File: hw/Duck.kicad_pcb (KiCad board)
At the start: 2 copper layers, 35.5 x 20.8 mm, 36 parts, among them J1 Conn_01x06, J2 Conn_01x04, J3 USB_C_Receptacle_USB2.0_14P, J4 Conn_01x06, Q1 MMBT3904, Q2 MMBT3904, U1 ESP32-S3-MINI-1, U2 SPX3819M5-L-3-3, U3 INMP441, U4 MAX17048G+T10, U5 CH343P

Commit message: hw: 🚧 Revision
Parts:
- added AE1: 2.4GHz 50R, Duck_footprints:ANT_IFA_USB_2.4GHz_50R, F.Cu at (58.6, 49.5)
- added C3: 1u, Capacitor_SMD:C_0402_1005Metric, F.Cu at (59.9, 53.4)
- added C4: 0 TBD, Capacitor_SMD:C_0402_1005Metric, F.Cu at (60.3, 46.5)
- added C5: 0 TBD, Capacitor_SMD:C_0402_1005Metric, F.Cu at (60.3, 49.2)
- added C6: 100n, Capacitor_SMD:C_0402_1005Metric, B.Cu at (66.3, 51.8)
- added C7: 6.8p, Capacitor_SMD:C_0402_1005Metric, B.Cu at (63.1, 57.9)
- added C8: 6.8p, Capacitor_SMD:C_0402_1005Metric, B.Cu at (66.8, 57.9)
- added L1: 0 TBD, Inductor_SMD:L_0402_1005Metric, F.Cu at (60.8, 47.9)
- added R1: 10k, Resistor_SMD:R_0402_1005Metric, F.Cu at (58.9, 53.4)
- added U2: PY32F003F1xU6, Package_DFN_QFN:QFN-20-1EP_3x3mm_P0.4mm_EP1.65x1.65mm, B.Cu at (64.8, 54.6)
- added Y1: 32MHz 12pF, Crystal:Crystal_SMD_2016-4Pin_2.0x1.6mm, B.Cu at (65.0, 58.0)
- BT1, C1, C2: moved to F.Cu
- C10: renamed from C4; moved to F.Cu
- C11: renamed from C5; moved to B.Cu
- C9: renamed from C3; moved to F.Cu
- D1: footprint LED_THT:LED_D5.0mm-4_RGB -> Duck_footprints:LED_1x04_D5.0_P1.27
- J2: footprint Duck_footprints:SMD_1x04_P2.54mm -> Duck_footprints:TestPoints_1x04_P2.0; moved to F.Cu
- R4: renamed from R3; moved to B.Cu
- R5: renamed from R4; moved to B.Cu
- R6: renamed from R5; moved to B.Cu
- U1: value ESP32-S3-MINI-1 -> ESP32-S3-PICO-1; footprint Espressif:ESP32-S3-MINI-1 -> Espressif:ESP32-S3-PICO-1-LGA-56
- U3: renamed from U2; moved to F.Cu
- U4: renamed from U3; moved to B.Cu
- moved J1 28.8 mm to (44.3, 44.8), turned to 0 degrees
- moved J2 17.5 mm to (41.1, 38.4), turned to 0 degrees
- moved C1 10.3 mm to (58.9, 51.6)
- moved C2 10.3 mm to (59.9, 51.6)
- moved C12 9.75 mm to (73.3, 53.5), turned to -90 degrees
- moved D1 9.32 mm to (71.4, 58.1)
- moved C10 8.51 mm to (72.8, 50.9), turned to -90 degrees
- moved C9 8.11 mm to (72.8, 52.8), turned to -90 degrees
- moved U1 7.32 mm to (64.0, 53.5)
- moved R4 6.92 mm to (69.6, 56.2)
- moved R5 6.92 mm to (71.4, 56.2)
- moved R6 6.92 mm to (73.3, 56.2)
- moved U5 6.15 mm to (71.2, 53.3), turned to 180 degrees
- moved R2 5.72 mm to (69.1, 53.8), turned to 90 degrees
- moved R3 5.04 mm to (68.2, 53.2), turned to 90 degrees
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- renumbered C6 to C12, C7 to C13, C8 to C14, C9 to C15, R9 to R10, R10 to R11, R1 to R2, R2 to R3, R6 to R7, R7 to R8, R8 to R9, U4 to U5, U5 to U6
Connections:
- J2 pad 3: /GNSS_TX -> /SWDIO
- J2 pad 4: /GNSS_RX -> /SWCLK
- U1 pad 1: GND -> Net-(U1-LNA_IN)
- U1 pad 12: /GNSS_TX -> unconnected-(U1-GPIO7-Pad12)
- U1 pad 13: /GNSS_RX -> unconnected-(U1-GPIO8-Pad13)
- U1 pad 16: /MIC_WS -> unconnected-(U1-GPIO11-Pad16)
- U1 pad 17: /MIC_SD -> unconnected-(U1-GPIO12-Pad17)
- U1 pad 18: /MIC_SCK -> unconnected-(U1-GPIO13-Pad18)
- U1 pad 19: /MIC_EN -> unconnected-(U1-GPIO14-Pad19)
- U1 pad 2: GND -> +3V3
- U1 pad 20: unconnected-(U1-GPIO16/U0CTS/ADC2_CH5/XTAL_32K_N-Pad20) -> +3V3
- U1 pad 21: /LED_R -> unconnected-(U1-GPIO15/XTAL_32K_P-Pad21)
- U1 pad 22: /LED_G -> unconnected-(U1-GPIO16/XTAL_32K_N-Pad22)
- U1 pad 25: /LED_B -> unconnected-(U1-USB_D-/GPIO19-Pad25)
- U1 pad 31: /SDA -> unconnected-(U1-SPIWP/NC-Pad31)
- U1 pad 32: /SCL -> unconnected-(U1-SPICS0/NC-Pad32)
- U1 pad 39: /U0TXD -> /SER_UP
- U1 pad 4: /BOOT0 -> /ESP_EN
- U1 pad 40: /U0RXD -> /SER_DN
- U1 pad 42: GND -> unconnected-(U1-GPIO37-Pad42)
- U1 pad 43: GND -> unconnected-(U1-GPIO38-Pad43)
- U1 pad 45: /ESP_EN -> unconnected-(U1-MTDO/GPIO40-Pad45)
- U1 pad 46: GND -> unconnected-(U1-VDD_CPU-Pad46)
- U1 pad 47: GND -> unconnected-(U1-MTDI/GPIO41-Pad47)
- U1 pad 48: GND -> unconnected-(U1-MTMS/GPIO42-Pad48)
- U1 pad 49: GND -> /U0TXD
- U1 pad 5: unconnected-(U1-GPIO1/TOUCH1/ADC1_CH0-Pad5) -> /BOOT0
- U1 pad 50: GND -> /U0RXD
- U1 pad 51: GND -> unconnected-(U1-GPIO45-Pad51)
- U1 pad 52: GND -> unconnected-(U1-GPIO46-Pad52)
- U1 pad 53: GND -> unconnected-(U1-XTAL_N/NC-Pad53)
- U1 pad 54: GND -> unconnected-(U1-XTAL_P/NC-Pad54)
- U1 pad 55: GND -> +3V3
- U1 pad 56: GND -> +3V3
- U4 pad 8: /MIC_EN -> +3V3
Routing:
- net +3V3: track 41.0 -> 2.71 mm, vias 2 -> 0
- net /BOOT0: track 32.5 -> 15.8 mm, vias 2 -> 0
- net +BATT: track 37.3 -> 23.8 mm, vias 2 -> 1
- net /MIC_EN: track 5.05 -> 0.00 mm
- net /SCL: track 5.63 -> 1.19 mm, vias 1 -> 0
- net /ESP_EN: track 17.9 -> 13.6 mm
- net /SDA: track 5.77 -> 2.13 mm, vias 1 -> 0
- net /U0TXD: track 16.6 -> 14.3 mm
- net Net-(D1-BK): track 2.18 -> 0.00 mm
- net /MIC_SCK: track 1.95 -> 0.00 mm
- net Net-(D1-GK): track 1.94 -> 0.00 mm
- net /MIC_SD: track 1.87 -> 0.00 mm
- net Net-(D1-RK): track 1.80 -> 0.00 mm
- net /MIC_WS: track 1.79 -> 0.00 mm
- net /U0RXD: track 14.4 -> 12.6 mm
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- removed copper zone on B.Cu, net +3V3

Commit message: hw: 🚧 Adjustments; layout?
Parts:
- removed C4, C5: 0 TBD, Capacitor_SMD:C_0402_1005Metric
- removed L1: 0 TBD, Inductor_SMD:L_0402_1005Metric
- removed R2, R3: 4.7k, Resistor_SMD:R_0402_1005Metric
- BT1: moved to B.Cu
- D1, R4, R5, R6: moved to F.Cu
- Y1: value 32MHz 12pF -> 24.576MHz 12pF
- moved C6 6.96 mm to (64.0, 58.4), turned to 0 degrees
- moved C8 6.66 mm to (62.9, 52.5), turned to -90 degrees
- moved C7 6.51 mm to (66.6, 52.5), turned to 90 degrees
- moved Y1 5.51 mm to (64.7, 52.5), turned to 0 degrees
- moved C12 3.22 mm to (70.4, 52.1), turned to 0 degrees
- moved U5 2.77 mm to (68.4, 53.1), turned to -90 degrees
- moved C1 2.17 mm to (60.0, 53.5)
- moved C2 2.17 mm to (60.9, 53.5)
- moved C3 2.17 mm to (60.9, 55.3)
- moved R1 2.17 mm to (60.0, 55.3)
- moved U1 2.17 mm to (65.1, 55.3)
- moved C10 1.99 mm to (73.5, 52.7)
- moved C9 1.99 mm to (73.5, 54.6)
- moved U3 1.99 mm to (71.0, 53.2)
- moved AE1 1.93 mm to (59.7, 51.1)
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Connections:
- AE1 pad 1: Net-(AE1-Pad1) -> Net-(U1-LNA_IN)
- U1 pad 27: unconnected-(U1-GPIO21-Pad27) -> /SER_DN
- U1 pad 36: unconnected-(U1-GPIO48/SPICLK_N-Pad36) -> /SER_UP
- U1 pad 39: /SER_UP -> unconnected-(U1-GPIO34-Pad39)
- U1 pad 40: /SER_DN -> unconnected-(U1-GPIO35-Pad40)
- U2 pad 1: /LED_R -> /LED_B
- U2 pad 10: /SER_UP -> /MIC_SCK
- U2 pad 11: /SER_DN -> unconnected-(U2-PB7-Pad11)
- U2 pad 12: unconnected-(U2-PF4-Pad12) -> /SDA
- U2 pad 15: unconnected-(U2-PF2-Pad15) -> /SCL
- U2 pad 16: /MIC_SD -> /SER_UP
- U2 pad 17: /MIC_SCK -> /SER_DN
- U2 pad 18: /SDA -> /LED_R
- U2 pad 19: /SCL -> unconnected-(U2-PA3-Pad19)
- U2 pad 2: /LED_B -> /MIC_SD
- U4 pad 4: +3V3 -> GND
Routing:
- net /MIC_SD: track 0.00 -> 12.8 mm
- net /SDA: track 2.13 -> 12.5 mm
- net /LED_B: track 0.00 -> 7.98 mm, vias 0 -> 1
- net /LED_R: track 0.00 -> 7.18 mm, vias 0 -> 1
- net /LED_G: track 0.00 -> 5.66 mm, vias 0 -> 1
- net /MIC_WS: track 0.00 -> 5.65 mm
- net +3V3: track 2.71 -> 7.90 mm
- net +BATT: track 23.8 -> 28.6 mm, vias 1 -> 0
- net /SER_DN: track 0.00 -> 4.18 mm, vias 0 -> 1
- net Net-(U1-LNA_IN): track 0.00 -> 4.10 mm
- net Net-(U2-PF0): track 0.00 -> 2.87 mm
- net Net-(D1-BK): track 0.00 -> 2.13 mm
- net Net-(D1-RK): track 0.00 -> 2.08 mm
- net /SER_UP: track 0.00 -> 2.01 mm, vias 0 -> 1
- net Net-(D1-GK): track 0.00 -> 1.94 mm
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
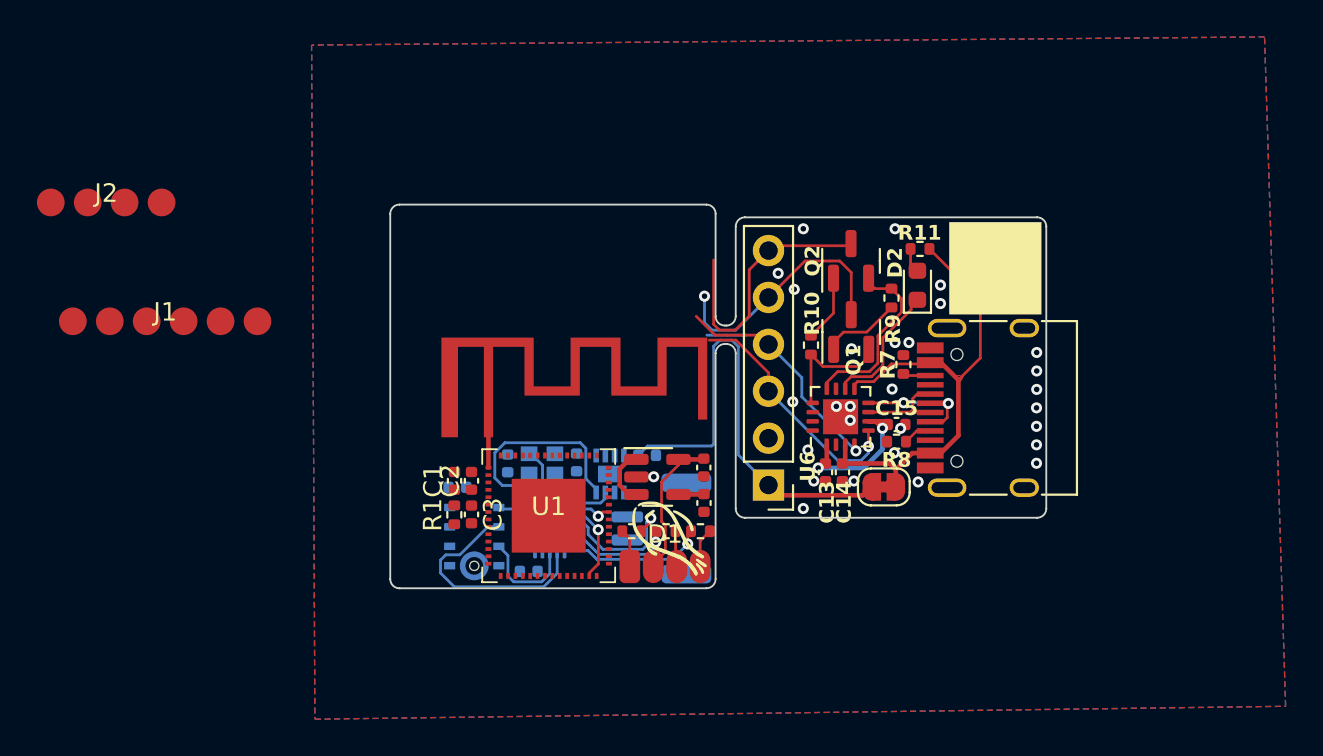
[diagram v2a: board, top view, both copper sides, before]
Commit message: hw: 🚧 Do we give up this small form factor?
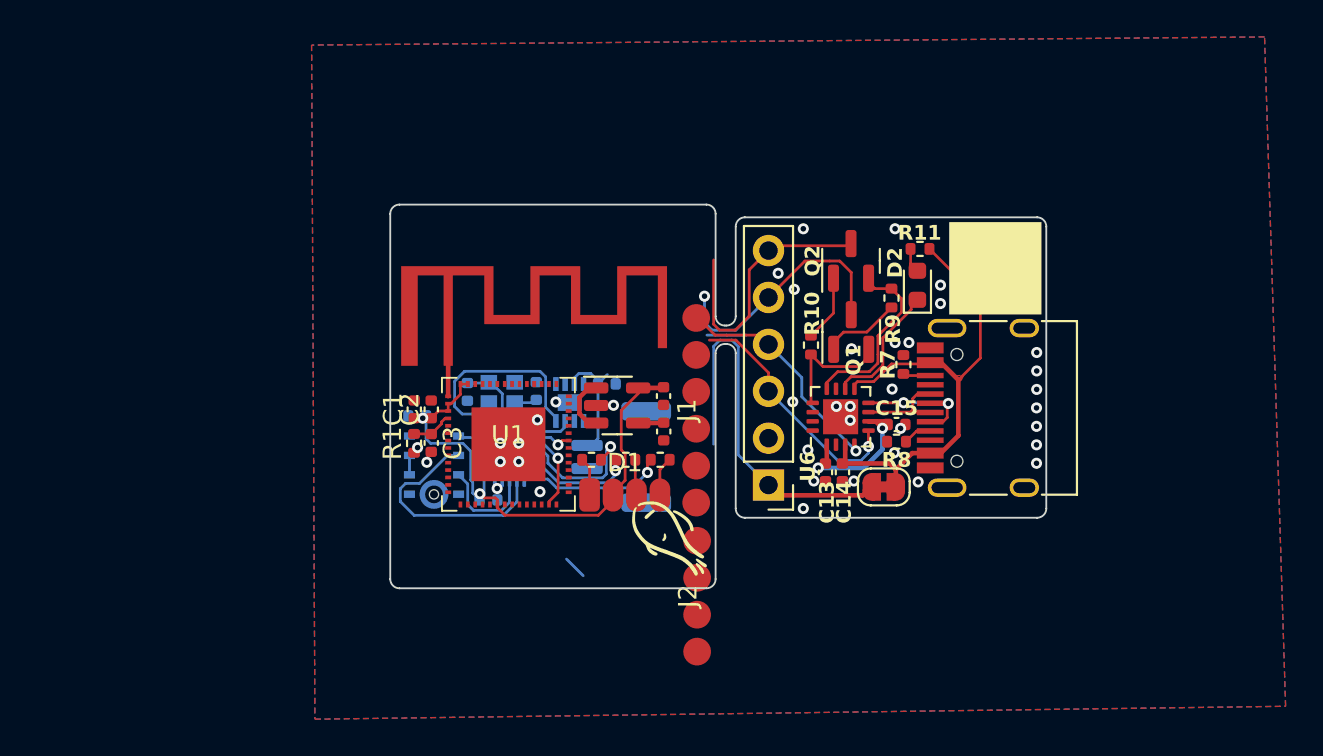
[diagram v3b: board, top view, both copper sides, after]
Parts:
- moved J2 38.5 mm to (73.1, 59.7), turned to 90 degrees
- moved J1 29.2 mm to (73.1, 49.6), turned to 90 degrees
- moved D1 4.44 mm to (69.2, 54.2)
- moved C1 4.44 mm to (57.8, 49.6)
- moved C11 4.44 mm to (58.0, 49.9)
- moved C2 4.44 mm to (58.7, 49.6)
- moved C3 4.44 mm to (58.7, 51.4)
- moved C8 4.44 mm to (60.7, 48.6)
- moved C10 4.44 mm to (71.3, 48.9)
- moved C12 4.44 mm to (68.2, 48.2)
- moved C9 4.44 mm to (71.3, 50.8)
- moved U5 4.44 mm to (66.2, 49.2)
- moved BT1 4.44 mm to (69.0, 52.2)
- moved U1 4.44 mm to (62.9, 51.5)
- moved U3 4.44 mm to (68.8, 49.4)
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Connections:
- U2 pad 5: unconnected-(U2-PA12-Pad5) -> GND
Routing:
- net +3V3: track 7.90 -> 31.6 mm, vias 0 -> 3
- net Net-(U2-PF1): track 0.00 -> 2.52 mm
- net /ESP_EN: track 13.6 -> 15.9 mm
- net /MIC_SD: track 12.8 -> 14.9 mm
- net GND: track 2.13 -> 0.00 mm, vias 29 -> 38
- net +BATT: track 28.6 -> 30.7 mm
- net Net-(U2-PF0): track 2.87 -> 4.04 mm

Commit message: hw: Further simplify 🚧
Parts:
- removed the C6 at (61.8, 54.5)
- removed the C7 at (64.4, 48.6)
- removed the C8 at (60.7, 48.6)
- removed the J2 at (73.1, 59.7)
- removed the U2 at (63.0, 51.9)
- removed Y1: 24.576MHz 12pF, Crystal:Crystal_SMD_2016-4Pin_2.0x1.6mm
- added R2: 4.7k, Resistor_SMD:R_0402_1005Metric, B.Cu at (65.2, 53.1)
- added R3: 4.7k, Resistor_SMD:R_0402_1005Metric, B.Cu at (64.7, 52.2)
- moved J1 4.09 mm to (73.1, 45.5)
- moved C7 2.14 mm to (66.6, 49.6), turned to -90 degrees
- moved U4 1.58 mm to (64.9, 50.1)
- moved R6 0.83 mm to (70.3, 52.1), turned to -90 degrees
- moved R4 0.36 mm to (67.7, 52.0), turned to -90 degrees
- moved BT1 0.34 mm to (68.9, 51.8)
- moved C6 0.27 mm to (58.0, 49.7)
- moved U3 0.27 mm to (58.9, 52.3)
- moved R5 0.26 mm to (69.4, 52.1), turned to -90 degrees
- moved D1 0.19 mm to (69.2, 54.0)
- moved R1 0.09 mm to (57.7, 51.4)
- renumbered C15 to C10, C9 to C4, C10 to C5, C11 to C6, C12 to C7, C13 to C8, C14 to C9, J4 to J2, U3 to U2, U4 to U3, U5 to U4, U6 to U5
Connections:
- U1 pad 25: unconnected-(U1-USB_D-/GPIO19-Pad25) -> /SDA
- U1 pad 26: unconnected-(U1-USB_D+/GPIO20-Pad26) -> /SCL
- U1 pad 27: /SER_DN -> unconnected-(U1-GPIO21-Pad27)
- U1 pad 36: /SER_UP -> /LED_B
- U1 pad 37: unconnected-(U1-GPIO47/SPICLK_P-Pad37) -> /LED_R
- U1 pad 38: unconnected-(U1-GPIO33-Pad38) -> /LED_G
- U1 pad 6: unconnected-(U1-GPIO1-Pad6) -> /MIC_SCK
- U1 pad 7: unconnected-(U1-GPIO2-Pad7) -> /MIC_SCK
- U1 pad 8: unconnected-(U1-GPIO3-Pad8) -> /MIC_SD
- U1 pad 9: unconnected-(U1-GPIO4-Pad9) -> /MIC_WS
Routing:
- net /MIC_SD: track 14.9 -> 1.18 mm, vias 0 -> 1
- net /SDA: track 12.5 -> 3.75 mm, vias 0 -> 1
- net /LED_R: track 7.18 -> 1.75 mm, vias 1 -> 0
- net /BOOT0: track 14.5 -> 19.4 mm
- net /MIC_WS: track 5.65 -> 1.15 mm, vias 0 -> 1
- net +3V3: track 31.6 -> 36.0 mm, vias 3 -> 4
- net /SER_DN: track 4.18 -> 0.00 mm, vias 1 -> 0
- net Net-(U2-PF0): track 4.04 -> 0.00 mm
- net /LED_B: track 7.98 -> 4.69 mm, vias 1 -> 0
- net Net-(U2-PF1): track 2.52 -> 0.00 mm
- net GND: track 0.00 -> 2.13 mm, vias 38 -> 32
- net /SER_UP: track 2.01 -> 0.00 mm, vias 1 -> 0
- net /LED_G: track 5.66 -> 3.68 mm, vias 1 -> 0
- net /ESP_EN: track 15.9 -> 17.2 mm
- net /U0TXD: track 13.3 -> 14.3 mm
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
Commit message: hw: Complete revision
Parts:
- removed JP1: SolderJumper_2_Bridged, Jumper:SolderJumper-2_P1.3mm_Bridged_RoundedPad1.0x1.5mm
- added C11: 1u, Capacitor_SMD:C_0402_1005Metric, F.Cu at (79.4, 41.7)
- added C12: 10n, Capacitor_SMD:C_0402_1005Metric, F.Cu at (85.9, 54.9)
- added C13: 4.7u, Capacitor_SMD:C_0402_1005Metric, F.Cu at (79.9, 54.2)
- added U6: SPX3819M5-L-3-3, Package_TO_SOT_SMD:SOT-23-5, F.Cu at (82.9, 53.6)
- J1: footprint Duck_footprints:TestPoints_1x06_P2.0 -> Duck_footprints:TestPoints_FFC_1x06_P0.5
- moved R1 16.4 mm to (73.2, 45.9), turned to -90 degrees
- moved AE1 16.0 mm to (73.3, 49.7), turned to 0 degrees
- moved C1 15.4 mm to (73.1, 47.8), turned to -90 degrees
- moved U3 15.2 mm to (72.0, 44.6), turned to 90 degrees
- moved C6 15.1 mm to (72.9, 47.2), turned to 0 degrees
- moved C3 14.5 mm to (72.2, 46.0), turned to 90 degrees
- moved C2 13.5 mm to (72.2, 47.8), turned to -90 degrees
- moved D1 13.4 mm to (61.7, 42.9), turned to 180 degrees
- moved C4 12.6 mm to (59.6, 46.2), turned to 90 degrees
- moved R6 12.1 mm to (60.5, 44.9), turned to 90 degrees
- moved C5 11.8 mm to (59.6, 48.1), turned to 90 degrees
- moved R5 10.7 mm to (61.5, 44.9), turned to 90 degrees
- moved BT1 9.66 mm to (62.0, 45.1), turned to 90 degrees
- moved R2 9.32 mm to (65.7, 43.8), turned to 0 degrees
- moved R4 8.38 mm to (63.2, 44.9), turned to 90 degrees
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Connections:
- J1 pad 1: +BATT -> +3V3
- J1 pad 2: GND -> /ESP_EN
- J1 pad 3: /U0TXD -> GND
- J1 pad 4: /U0RXD -> /BOOT0
- J1 pad 5: /ESP_EN -> /U0RXD
- J1 pad 6: /BOOT0 -> /U0TXD
- J2 pad 1: +BATT -> +3V3
- J2 pad 2: GND -> /ESP_EN
- J2 pad 3: /U0TXD -> GND
- J2 pad 4: /U0RXD -> /BOOT0
- J2 pad 5: /ESP_EN -> /U0RXD
- J2 pad 6: /BOOT0 -> /U0TXD
- U1 pad 14: unconnected-(U1-GPIO9-Pad14) -> /U0RXD
- U1 pad 22: unconnected-(U1-GPIO16/XTAL_32K_N-Pad22) -> /U0TXD
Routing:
- net +3V3: track 36.0 -> 58.7 mm
- net +BATT: track 31.0 -> 9.27 mm, vias 2 -> 1
- net /U0TXD: track 14.3 -> 31.4 mm, vias 1 -> 3
- net /ESP_EN: track 17.2 -> 31.4 mm, vias 1 -> 0
- net /U0RXD: track 12.6 -> 25.6 mm, vias 1 -> 3
- net GND: track 2.13 -> 4.32 mm, vias 32 -> 33
- net VBUS: track 27.7 -> 29.8 mm
- net Net-(U6-BP): track 0.00 -> 1.50 mm
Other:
- board size 35.5 x 20.8 mm -> 35.6 x 20.8 mm

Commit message: hw: Most of the polish
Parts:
- moved G*** 11.6 mm to (61.3, 51.6), turned to 180 degrees
- moved AE1 0.50 mm to (73.3, 49.2)
- moved C13 0.18 mm to (79.9, 54.0)
- moved BT1 0.10 mm to (62.1, 45.1)
- moved C4 0.10 mm to (59.7, 46.2)
- moved C5 0.10 mm to (59.7, 48.1)
- moved D1 0.10 mm to (61.8, 42.9)
- moved R4 0.10 mm to (63.3, 44.9)
- moved R5 0.10 mm to (61.6, 44.9)
- moved R6 0.10 mm to (60.6, 44.9)
- moved U2 0.10 mm to (62.2, 47.6)
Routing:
- net Net-(U1-LNA_IN): track 4.10 -> 3.60 mm
- net GND: track 4.32 -> 4.10 mm, vias 33 -> 62
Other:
- board size 35.6 x 20.8 mm -> 33.1 x 16.3 mm

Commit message: hw: Hopefully all finished; polish in the details to-do
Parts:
- moved BT1 0.31 mm to (62.1, 44.8)
- moved C1 0.31 mm to (73.1, 47.5)
- moved C2 0.31 mm to (72.2, 47.5)
- moved C3 0.31 mm to (72.2, 45.6)
- moved C4 0.31 mm to (59.7, 45.9)
- moved C5 0.31 mm to (59.7, 47.8)
- moved C6 0.31 mm to (72.9, 46.9)
- moved C7 0.31 mm to (64.3, 47.1)
- moved D1 0.31 mm to (61.8, 42.6)
- moved G*** 0.31 mm to (61.3, 51.2)
- moved J1 0.31 mm to (73.2, 43.1)
- moved R3 0.31 mm to (66.2, 44.5)
- moved R4 0.31 mm to (63.3, 44.6)
- moved R5 0.31 mm to (61.6, 44.6)
- moved U1 0.31 mm to (68.0, 45.2)
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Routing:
- net /U0RXD: track 25.6 -> 26.4 mm
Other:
- outline, holes or cut-outs redrawn

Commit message: hw: Finalize PCB details
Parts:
- G***: moved to B.Cu
- moved G*** 10.6 mm to (71.8, 52.3), turned to 0 degrees
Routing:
- net GND: track 4.09 -> 0.06 mm, vias 62 -> 66
- net /ESP_EN: track 31.3 -> 31.9 mm
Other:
- board text added: "<24-"
- board text added: "Rev. 2"
- board text added: "大雪"
- board text removed: "<24-Flurry"
- board text removed: "Rev. 1"
